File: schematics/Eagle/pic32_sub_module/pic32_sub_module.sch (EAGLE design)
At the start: 2 parts, among them U1 PIC32MZ2048EFG144-I/PH

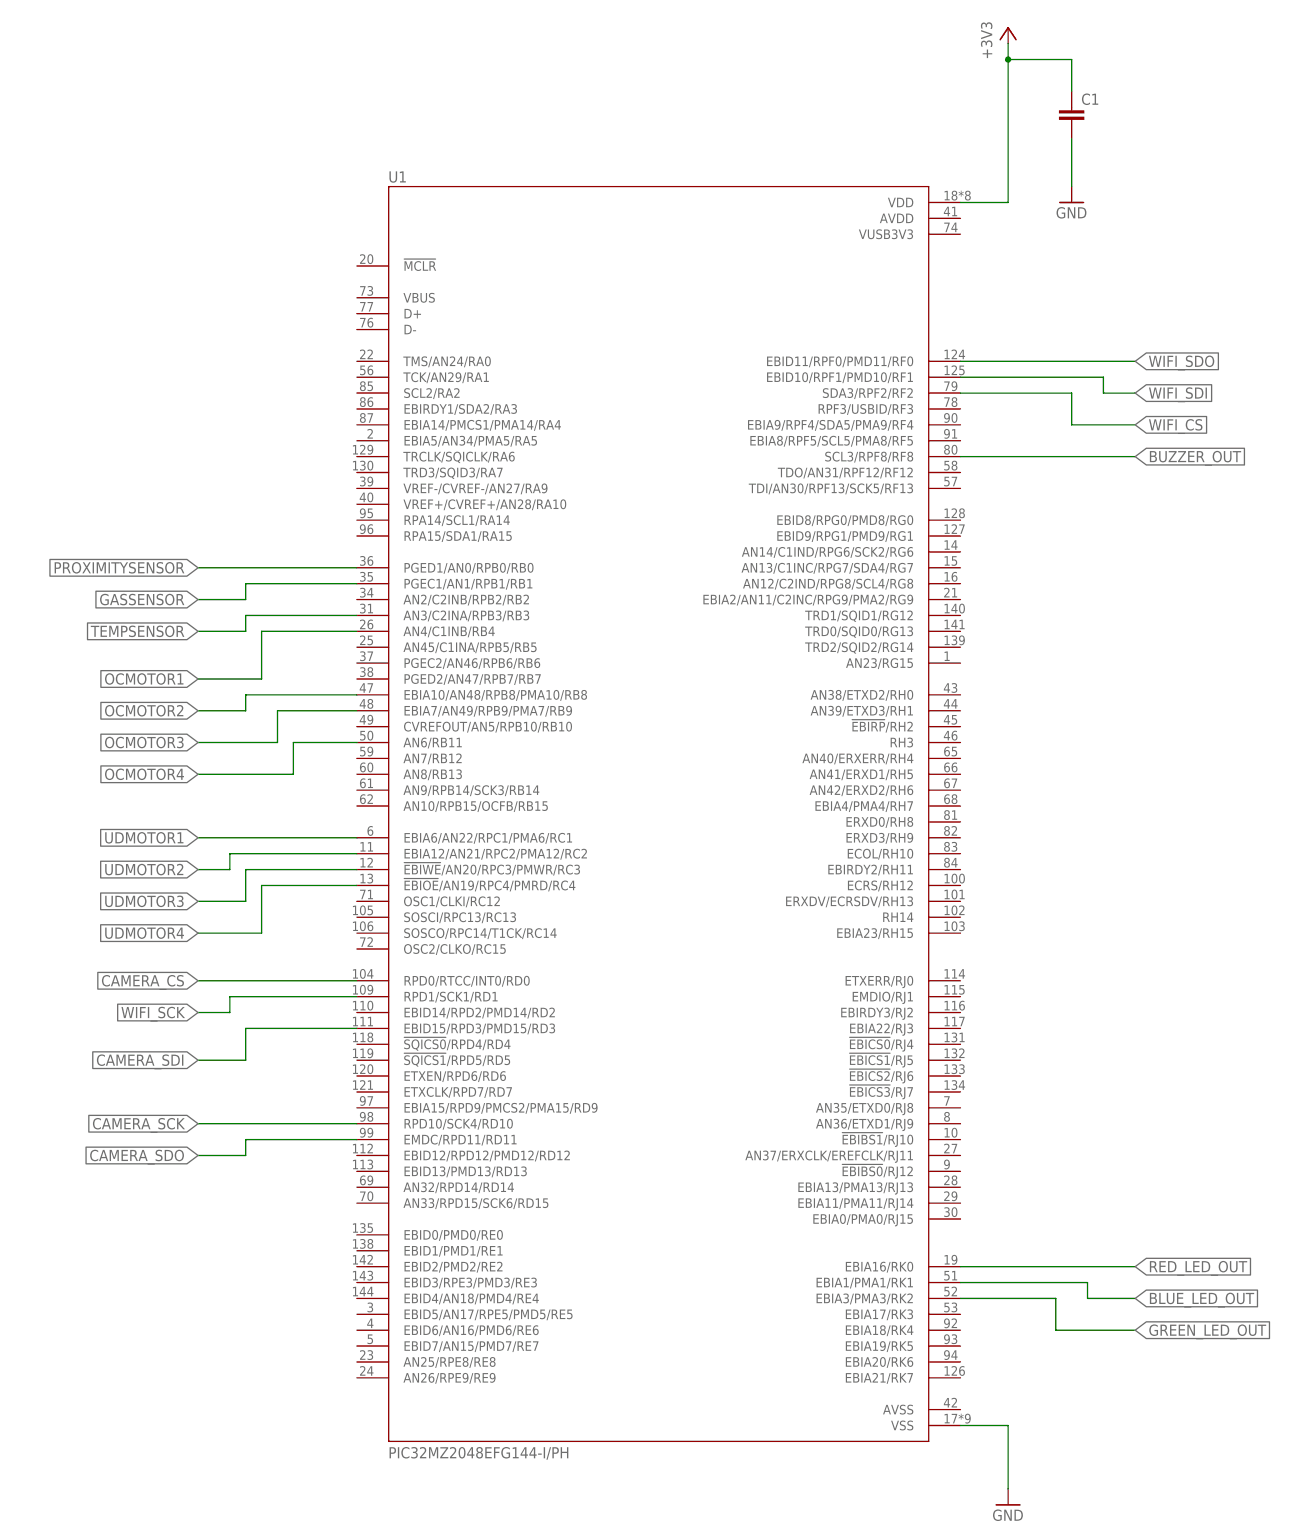
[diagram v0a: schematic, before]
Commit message: updated schematics and uart routine
pinout errors so had to correct.

updated pintouts to reflect current board
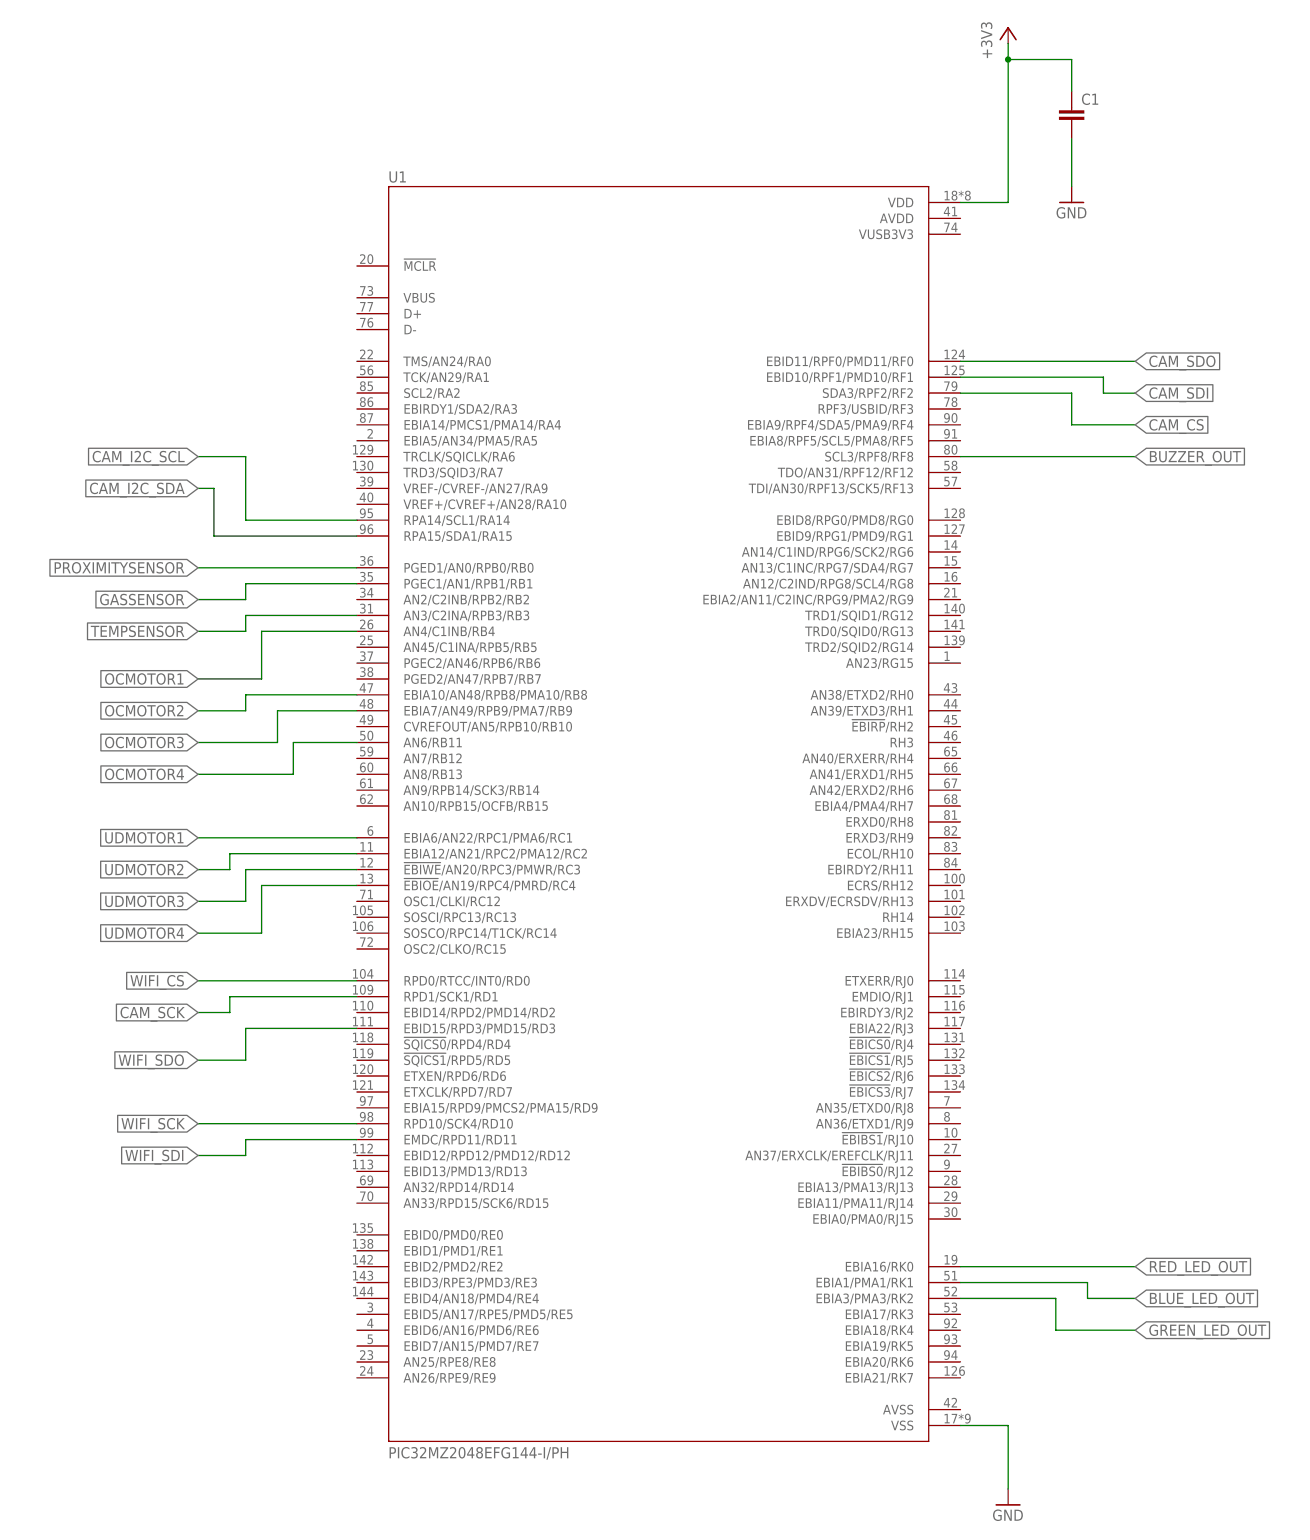
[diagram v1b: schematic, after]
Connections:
- removed net CAMERA_CS: U1.RPD0/RTCC/INT0/RD0
- removed net CAMERA_SCK: U1.RPD10/SCK4/RD10
- removed net CAMERA_SDI: U1.EBID15/RPD3/PMD15/RD3
- removed net CAMERA_SDO: U1.EMDC/RPD11/RD11
- new net CAM_CS: U1.SDA3/RPF2/RF2
- new net CAM_I2C_SCL: U1.RPA14/SCL1/RA14
- new net CAM_I2C_SDA: U1.RPA15/SDA1/RA15
- new net CAM_SCK: U1.RPD1/SCK1/RD1
- new net CAM_SDI: U1.EBID10/RPF1/PMD10/RF1
- new net CAM_SDO: U1.EBID11/RPF0/PMD11/RF0
- net WIFI_CS: now also U1.RPD0/RTCC/INT0/RD0; no longer U1.SDA3/RPF2/RF2
- net WIFI_SCK: now also U1.RPD10/SCK4/RD10; no longer U1.RPD1/SCK1/RD1
- net WIFI_SDI: now also U1.EMDC/RPD11/RD11; no longer U1.EBID10/RPF1/PMD10/RF1
- net WIFI_SDO: now also U1.EBID15/RPD3/PMD15/RD3; no longer U1.EBID11/RPF0/PMD11/RF0
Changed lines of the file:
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@@
 </segment>
 </net>
-<net name="CAMERA_SCK" class="0">
+<net name="WIFI_SCK" class="0">
 <segment>
 <pinref part="U1" gate="G$1" pin="RPD10/SCK4/RD10"/>
@@
 </segment>
 </net>
-<net name="CAMERA_SDO" class="0">
+<net name="WIFI_SDI" class="0">
 <segment>
 <pinref part="U1" gate="G$1" pin="EMDC/RPD11/RD11"/>
@@
 </segment>
 </net>
-<net name="CAMERA_SDI" class="0">
+<net name="WIFI_SDO" class="0">
 <segment>
 <pinref part="U1" gate="G$1" pin="EBID15/RPD3/PMD15/RD3"/>
@@
 </segment>
 </net>
-<net name="CAMERA_CS" class="0">
+<net name="WIFI_CS" class="0">
 <segment>
 <pinref part="U1" gate="G$1" pin="RPD0/RTCC/INT0/RD0"/>
@@
 </segment>
 </net>
-<net name="WIFI_SCK" class="0">
+<net name="CAM_SCK" class="0">
 <segment>
 <pinref part="U1" gate="G$1" pin="RPD1/SCK1/RD1"/>
@@
 </segment>
 </net>
-<net name="WIFI_SDO" class="0">
+<net name="CAM_SDO" class="0">
 <segment>
 <pinref part="U1" gate="G$1" pin="EBID11/RPF0/PMD11/RF0"/>
@@
 </segment>
 </net>
-<net name="WIFI_SDI" class="0">
+<net name="CAM_SDI" class="0">
 <segment>
 <pinref part="U1" gate="G$1" pin="EBID10/RPF1/PMD10/RF1"/>
@@
 </segment>
 </net>
-<net name="WIFI_CS" class="0">
+<net name="CAM_CS" class="0">
 <segment>
 <pinref part="U1" gate="G$1" pin="SDA3/RPF2/RF2"/>
@@
 </segment>
 </net>
+<net name="CAM_I2C_SCL" class="0">
+<segment>
+<pinref part="U1" gate="G$1" pin="RPA14/SCL1/RA14"/>
+<wire x1="-48.26" y1="78.74" x2="-66.04" y2="78.74" width="0.1524" layer="91"/>
+<wire x1="-66.04" y1="78.74" x2="-66.04" y2="88.9" width="0.1524" layer="91"/>
+<wire x1="-66.04" y1="88.9" x2="-73.66" y2="88.9" width="0.1524" layer="91"/>
+<label x="-73.66" y="88.9" size="1.778" layer="95" rot="R180" xref="yes"/>
+</segment>
+</net>
+<net name="CAM_I2C_SDA" class="0">
+<segment>
+<pinref part="U1" gate="G$1" pin="RPA15/SDA1/RA15"/>
+<wire x1="-48.26" y1="76.2" x2="-71.12" y2="76.2" width="0.1524" layer="91"/>
+<wire x1="-71.12" y1="76.2" x2="-71.12" y2="83.82" width="0.1524" layer="91"/>
+<wire x1="-71.12" y1="83.82" x2="-73.66" y2="83.82" width="0.1524" layer="91"/>
+<label x="-73.66" y="83.82" size="1.778" layer="95" rot="R180" xref="yes"/>
+</segment>
+</net>
